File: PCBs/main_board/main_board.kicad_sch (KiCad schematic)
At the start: 20 parts, among them J1 MS5803, J10 NEO-6M, J11 Limit_b, J12 Limit_p, J15 Conn_01x03, J2 I2C, J4 Batt, J5 OV5642, J6 JST_B, J7 JST_P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

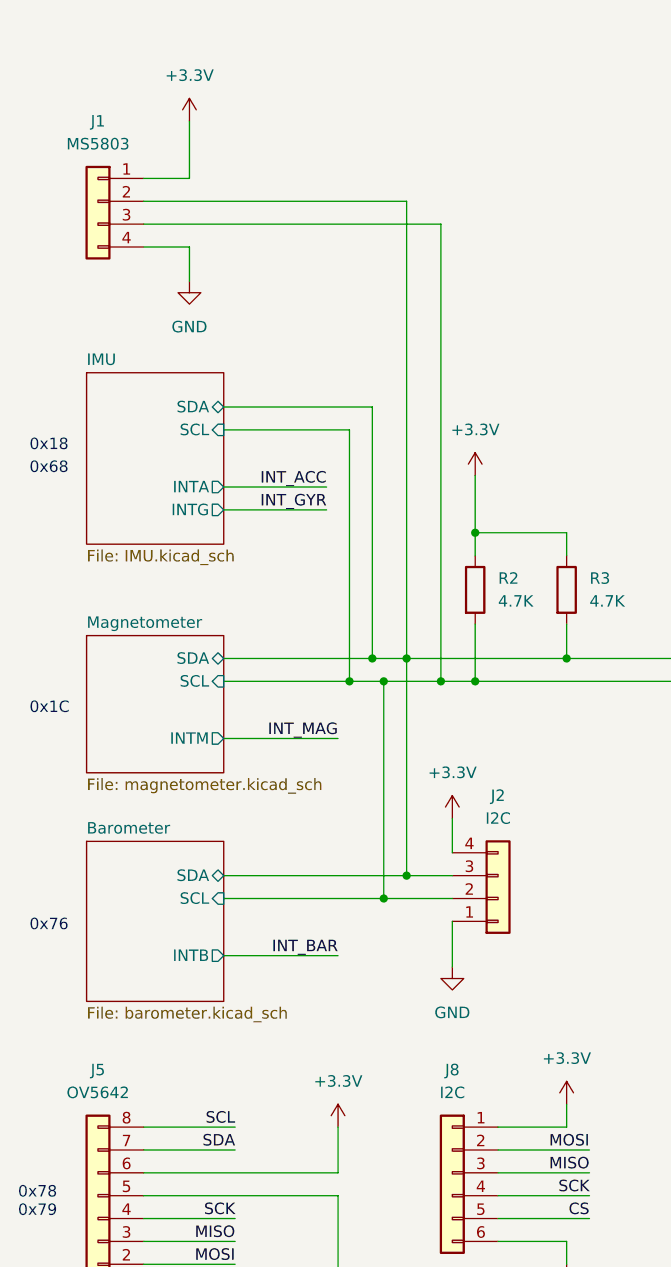
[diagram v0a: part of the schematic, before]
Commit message: updated schematic 3d models
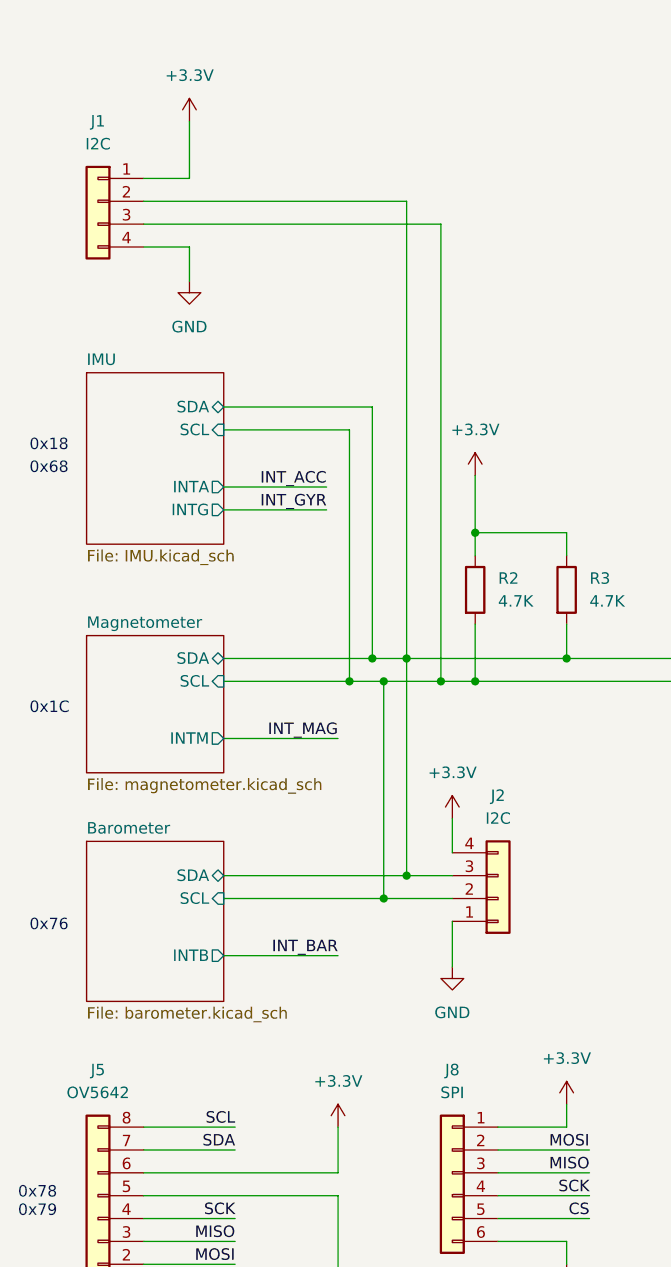
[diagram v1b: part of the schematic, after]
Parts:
- J1: value MS5803 -> I2C
- J8: value I2C -> SPI
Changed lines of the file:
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@@
     (in_bom yes) (on_board yes) (fields_autoplaced)
     (property "Reference" "J1" (id 0) (at 53.34 45.72 0))
-    (property "Value" "MS5803" (id 1) (at 53.34 48.26 0))
+    (property "Value" "I2C" (id 1) (at 53.34 48.26 0))
     (property "Footprint" "Connector_JST:JST_EH_B4B-EH-A_1x04_P2.50mm_Vertical" (id 2) (at 53.34 54.61 0)
       (effects (font (size 1.27 1.27)) hide)
@@
     (in_bom yes) (on_board yes) (fields_autoplaced)
     (property "Reference" "J8" (id 0) (at 92.71 151.13 0))
-    (property "Value" "I2C" (id 1) (at 92.71 153.67 0))
+    (property "Value" "SPI" (id 1) (at 92.71 153.67 0))
     (property "Footprint" "Connector_PinHeader_2.54mm:PinHeader_1x06_P2.54mm_Vertical" (id 2) (at 92.71 162.56 0)
       (effects (font (size 1.27 1.27)) hide)
@@
     )
     (path "/1f59985f-a35e-4b77-a6bb-f2653a188625"
-      (reference "J1") (unit 1) (value "MS5803") (footprint "Connector_JST:JST_EH_B4B-EH-A_1x04_P2.50mm_Vertical")
+      (reference "J1") (unit 1) (value "I2C") (footprint "Connector_JST:JST_EH_B4B-EH-A_1x04_P2.50mm_Vertical")
     )
     (path "/5717034c-0d15-44b4-ba92-6a7611562e6f"
@@
     )
     (path "/7aabbbfb-9beb-40df-9d78-52f2b2efad83"
-      (reference "J8") (unit 1) (value "I2C") (footprint "Connector_PinHeader_2.54mm:PinHeader_1x06_P2.54mm_Vertical")
+      (reference "J8") (unit 1) (value "SPI") (footprint "Connector_PinHeader_2.54mm:PinHeader_1x06_P2.54mm_Vertical")
     )
     (path "/1dba2aaa-e042-4434-844d-2dabdc52fc5a"

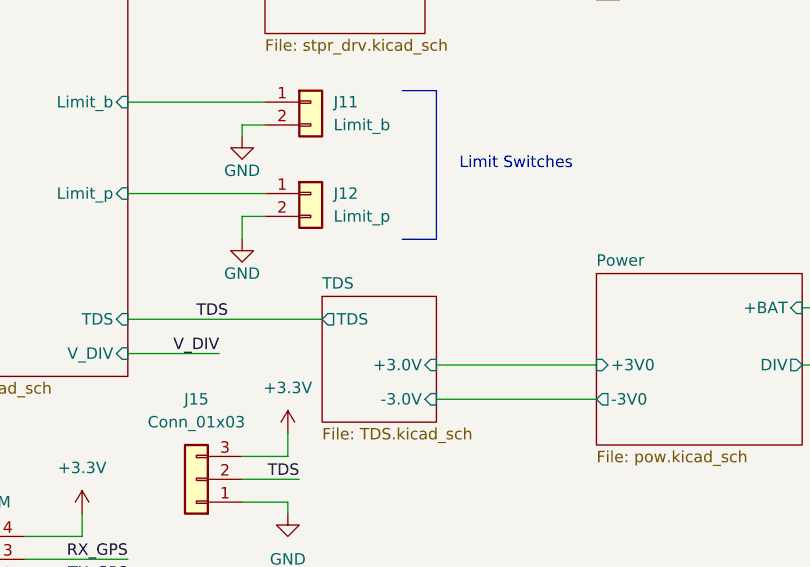
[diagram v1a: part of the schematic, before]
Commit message: updated schematic labels
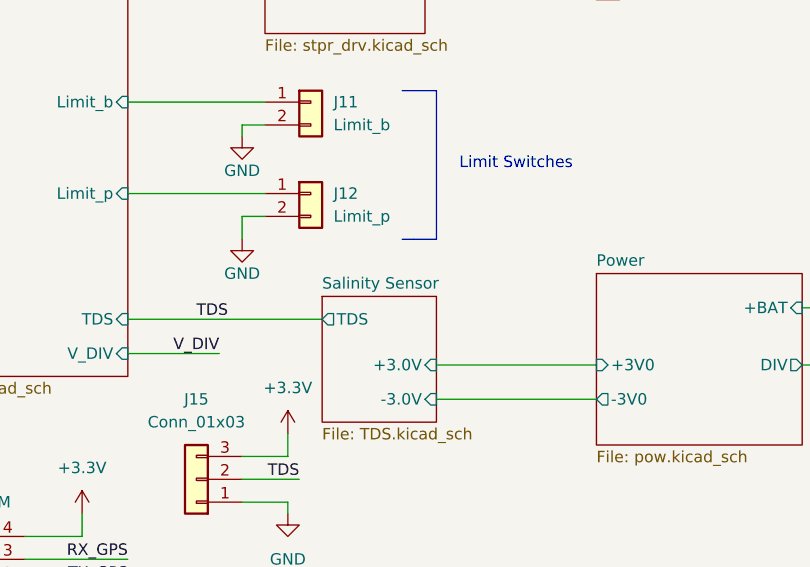
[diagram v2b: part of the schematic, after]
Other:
- sheet TDS renamed Salinity Sensor
- title: (none) -> OceanAI
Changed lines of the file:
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@@
 (kicad_sch (version 20211123) (generator eeschema)
   (paper "A4")
+  (title_block
+    (title "OceanAI")
+    (date "2022-07-25")
+    (rev "2")
+  )
   (junction (at 91.44 107.95) (diameter 0) (color 0 0 0 0)
   )
@@
     (stroke (width 0.1524) (type solid) (color 0 0 0 0))
     (fill (color 0 0 0 0.0000))
-    (property "Sheet name" "TDS" (id 0) (at 191.77 135.1784 0)
+    (property "Sheet name" "Salinity Sensor" (id 0) (at 191.77 135.1784 0)
       (effects (font (size 1.27 1.27)) (justify left bottom))
     )
